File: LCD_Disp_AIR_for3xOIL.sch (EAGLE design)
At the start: 35 parts, among them IC3 TC10553.3V, J1 12V input, Q1 16MHz, SW1 ENCODER_SW1-PEC12, U1 ATMEGA328P-AU(R), U3 78M05

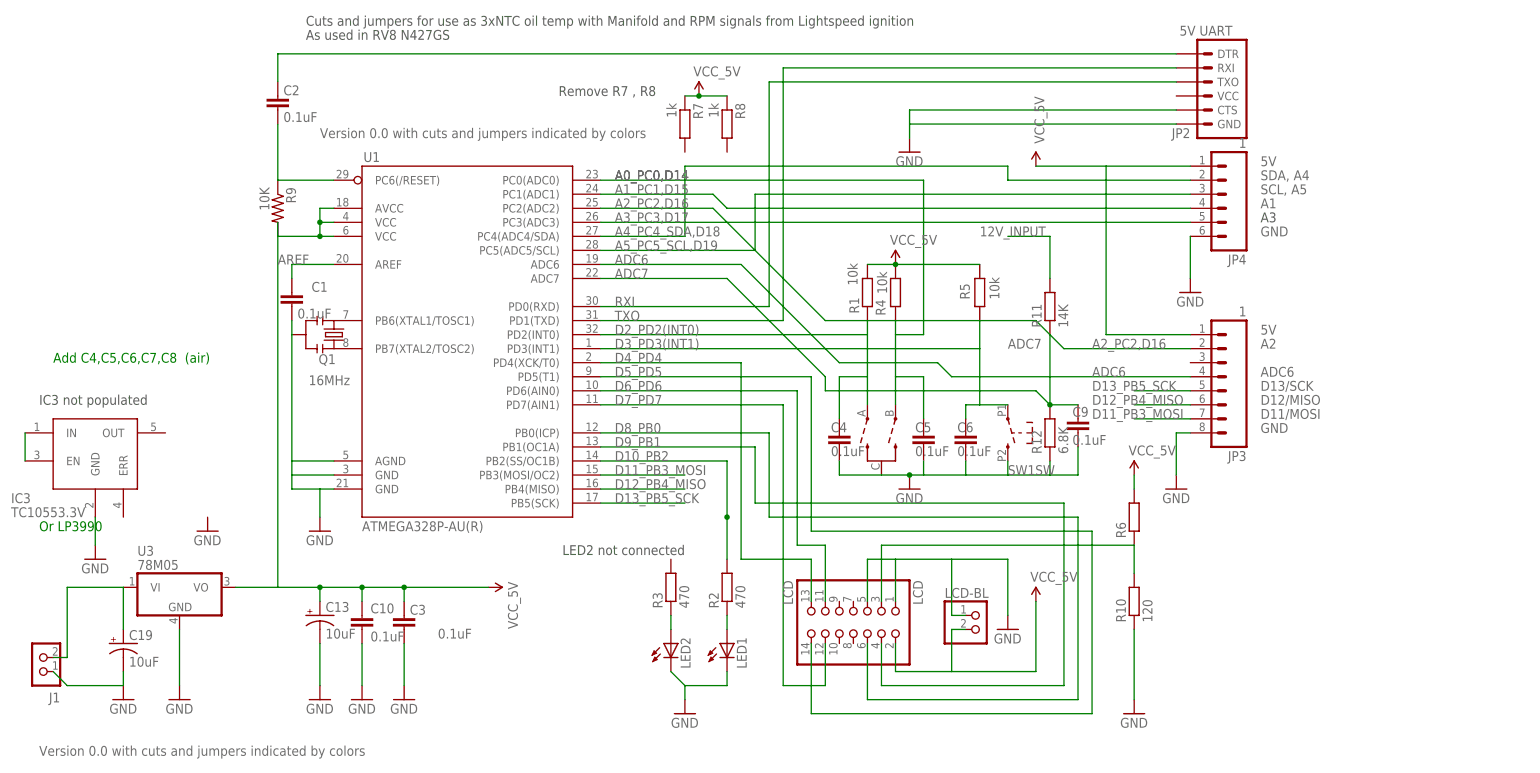
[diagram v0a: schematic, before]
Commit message: Removed MP display and replaced it with Fuel pressure. Added external alarm output to hardware. reworked code so that multiple alarms can be indicated reordered the menu so that the most important display items are at each end of the list. (knob all the way to the left or right) added a copy of the schematics to this git added the excel sheets with the fuel pressure calibration points and curve fitting outputs
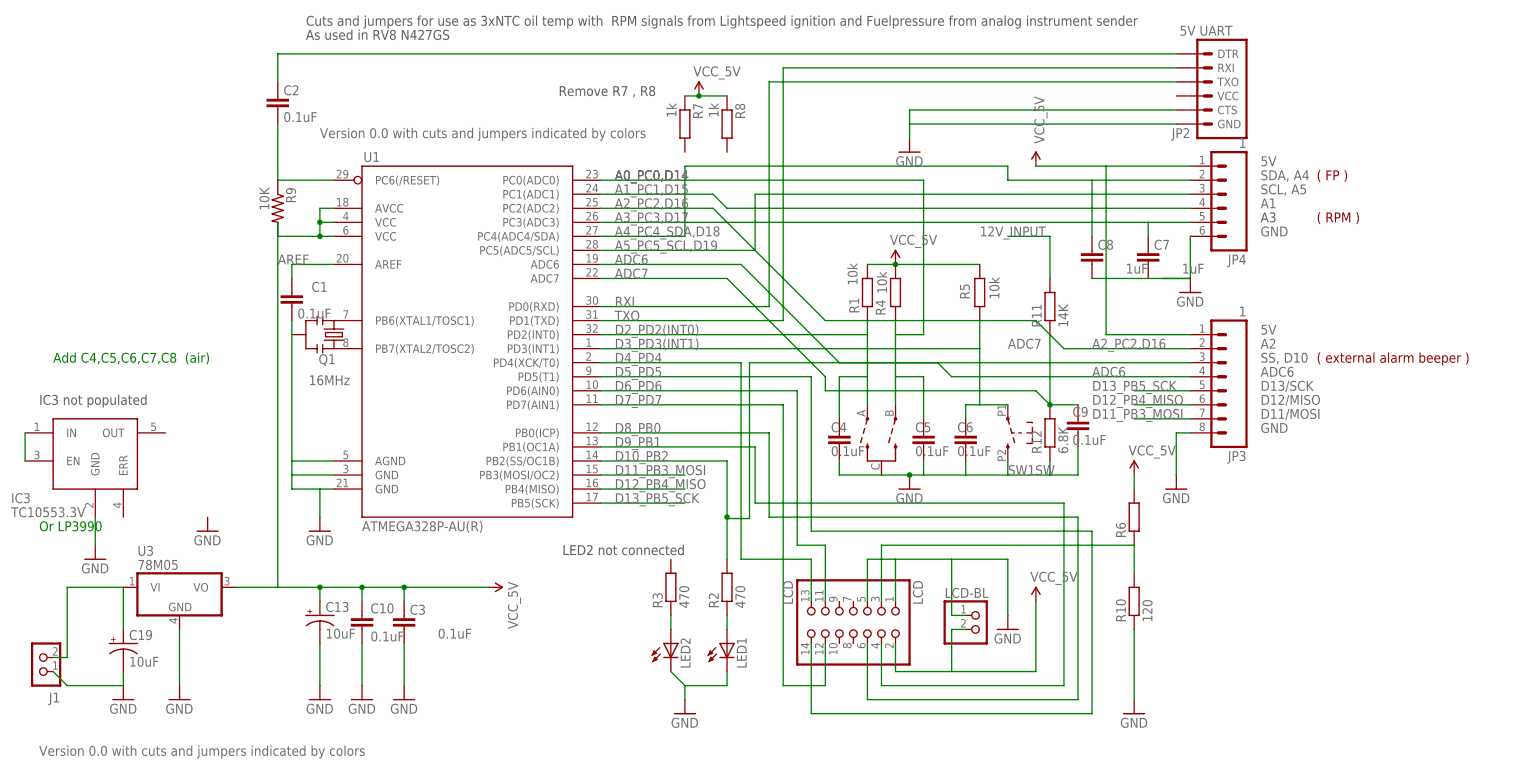
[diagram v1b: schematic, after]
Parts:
- added C7, C8: 1uF, SparkFun:CAP0805
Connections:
- new net N$3: C7.1, C8.1
- net A3_PC3,D17: now also C7.2
- net A4_PC4_SDA,D18: now also C8.2
- net D10_PB2: now also JP3.3
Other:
- note added: "( FP )"
- note added: "( RPM )"
- note added: "( external alarm beeper )"
- note added: "Cuts and jumpers for use as 3xNTC oil temp with RPM signals from Lightspeed ignition and Fuelpressure from analog instrument sender"
- note added: "SS, D10"
- note removed: "Cuts and jumpers for use as 3xNTC oil temp with Manifold and RPM signals from Lightspeed ignition"
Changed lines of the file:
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@@
 <?xml version="1.0" encoding="utf-8"?>
 <!DOCTYPE eagle SYSTEM "eagle.dtd">
-<eagle version="6.5.0">
+<eagle version="6.4">
 <drawing>
 <settings>
@@
 <part name="IC3" library="1AA_Stofer" deviceset="TC10553.3V" device=""/>
 <part name="LCD-BL" library="1AA_Stofer" deviceset="PINHD-1X2" device=""/>
+<part name="C7" library="SparkFun" deviceset="CAP" device="0805" value="1uF"/>
+<part name="C8" library="SparkFun" deviceset="CAP" device="0805" value="1uF"/>
 </parts>
 <sheets>
@@
 <text x="-5.08" y="157.48" size="1.778" layer="91">Add C4,C5,C6,C7,C8  (air)</text>
 <text x="-7.62" y="127" size="1.778" layer="91">Or LP3990</text>
-<wire x1="180.34" y1="157.48" x2="200.66" y2="157.48" width="0.1524" layer="109"/>
 <wire x1="106.68" y1="121.92" x2="111.76" y2="121.92" width="0.1524" layer="109"/>
 <wire x1="111.76" y1="121.92" x2="111.76" y2="137.16" width="0.1524" layer="109"/>
@@
 <text x="213.36" y="182.88" size="1.778" layer="97">A3</text>
 <text x="109.22" y="124.46" size="1.778" layer="97" rot="R180">LED2 not connected </text>
-<text x="40.64" y="218.44" size="1.778" layer="97">Cuts and jumpers for use as 3xNTC oil temp with Manifold and RPM signals from Lightspeed ignition</text>
+<text x="40.64" y="218.44" size="1.778" layer="97">Cuts and jumpers for use as 3xNTC oil temp with  RPM signals from Lightspeed ignition and Fuelpressure from analog instrument sender</text>
 <text x="40.64" y="215.9" size="1.778" layer="97">As used in RV8 N427GS</text>
 <text x="-7.62" y="149.86" size="1.778" layer="97">IC3 not populated</text>
+<text x="213.36" y="157.48" size="1.778" layer="95">SS, D10</text>
+<text x="223.52" y="190.5" size="1.778" layer="94">( FP )</text>
+<text x="223.52" y="182.88" size="1.778" layer="94">( RPM )</text>
+<text x="223.52" y="157.48" size="1.778" layer="94">( external alarm beeper )</text>
 </plain>
 <instances>
@@
 <instance part="IC3" gate="G$1" x="2.54" y="139.7"/>
 <instance part="LCD-BL" gate="G$1" x="162.56" y="109.22"/>
+<instance part="C7" gate="G$1" x="193.04" y="177.8" smashed="yes" rot="R180">
+<attribute name="NAME" x="194.056" y="177.927" size="1.778" layer="95"/>
+<attribute name="VALUE" x="199.136" y="173.609" size="1.778" layer="96"/>
+</instance>
+<instance part="C8" gate="G$1" x="182.88" y="177.8" smashed="yes" rot="R180">
+<attribute name="NAME" x="183.896" y="177.927" size="1.778" layer="95"/>
+<attribute name="VALUE" x="188.976" y="173.609" size="1.778" layer="96"/>
+</instance>
 </instances>
 <busses>
@@
 <pinref part="JP4" gate="G$1" pin="6"/>
 <wire x1="200.66" y1="180.34" x2="200.66" y2="172.72" width="0.1524" layer="91"/>
+<wire x1="200.66" y1="172.72" x2="195.58" y2="172.72" width="0.1524" layer="91"/>
 </segment>
 <segment>
@@
 <wire x1="167.64" y1="193.04" x2="167.64" y2="190.5" width="0.1524" layer="91"/>
 <pinref part="JP4" gate="G$1" pin="2"/>
-<wire x1="167.64" y1="190.5" x2="200.66" y2="190.5" width="0.1524" layer="91"/>
+<wire x1="167.64" y1="190.5" x2="182.88" y2="190.5" width="0.1524" layer="91"/>
+<pinref part="C8" gate="G$1" pin="2"/>
+<wire x1="182.88" y1="190.5" x2="200.66" y2="190.5" width="0.1524" layer="91"/>
+<wire x1="182.88" y1="180.34" x2="182.88" y2="190.5" width="0.1524" layer="91"/>
 </segment>
 </net>
@@
 <pinref part="R2" gate="G$1" pin="2"/>
 <junction x="116.84" y="129.54"/>
-<wire x1="116.84" y1="129.54" x2="116.84" y2="121.92" width="0.1524" layer="91"/>
+<wire x1="116.84" y1="129.54" x2="116.84" y2="129.286" width="0.1524" layer="91"/>
+<pinref part="JP3" gate="G$1" pin="3"/>
+<wire x1="116.84" y1="129.286" x2="116.84" y2="121.92" width="0.1524" layer="91"/>
+<wire x1="200.66" y1="157.48" x2="120.904" y2="157.48" width="0.1524" layer="91"/>
+<wire x1="120.904" y1="157.48" x2="120.904" y2="129.286" width="0.1524" layer="91"/>
+<wire x1="120.904" y1="129.286" x2="116.84" y2="129.286" width="0.1524" layer="91"/>
 </segment>
 </net>
@@
 <label x="96.52" y="182.88" size="1.778" layer="95"/>
 <pinref part="JP4" gate="G$1" pin="5"/>
-<wire x1="93.98" y1="182.88" x2="200.66" y2="182.88" width="0.1524" layer="91"/>
+<wire x1="93.98" y1="182.88" x2="193.04" y2="182.88" width="0.1524" layer="91"/>
+<pinref part="C7" gate="G$1" pin="2"/>
+<wire x1="193.04" y1="182.88" x2="200.66" y2="182.88" width="0.1524" layer="91"/>
+<wire x1="193.04" y1="180.34" x2="193.04" y2="182.88" width="0.1524" layer="91"/>
 </segment>
 </net>
@@
 </segment>
 </net>
+<net name="N$3" class="0">
+<segment>
+<pinref part="C8" gate="G$1" pin="1"/>
+<pinref part="C7" gate="G$1" pin="1"/>
+<wire x1="182.88" y1="172.72" x2="193.04" y2="172.72" width="0.1524" layer="91"/>
+<wire x1="193.04" y1="172.72" x2="200.66" y2="172.72" width="0.1524" layer="91"/>
+</segment>
+</net>
